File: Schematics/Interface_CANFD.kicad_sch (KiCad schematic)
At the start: 4 parts, among them U8 TCAN1044AVDRQ1

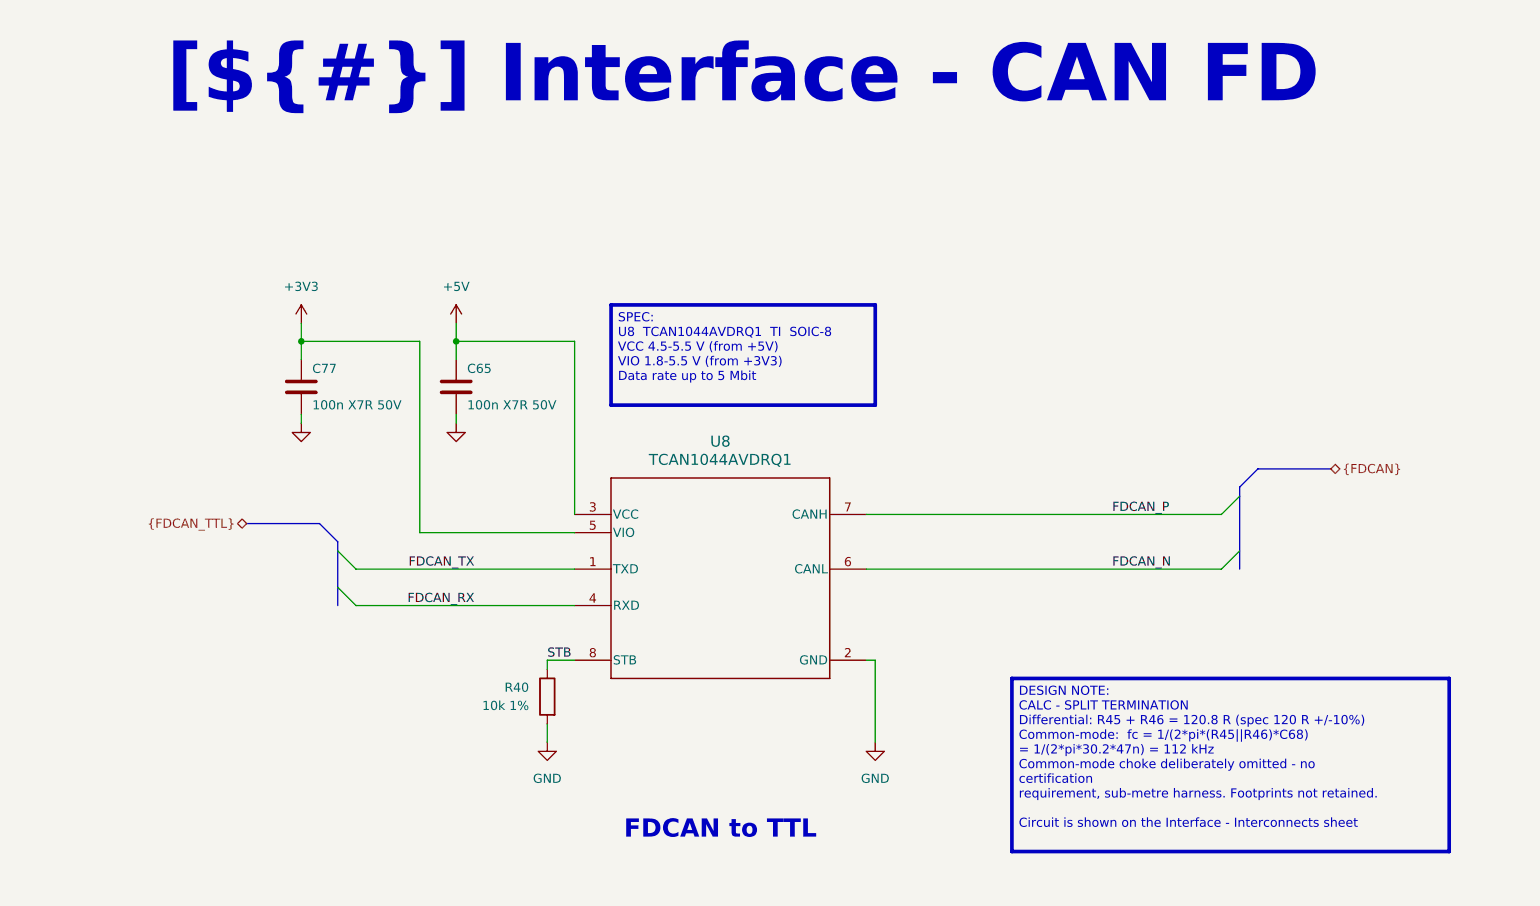
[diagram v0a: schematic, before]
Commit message: Clean up schematic design notes; export schematic and PCB artwork PDFs
- Remove firmware-only notes (boot sequence, calibration procedure,
  firmware SPI/PWM settings) and template/empty text; keep hardware facts
- Tighten wording of all DESIGN/SPEC/ASSEMBLY/REV 1 notes and resize
  boxes so no note text wraps or overflows
- Re-export schematic PDF
- Add PCB artwork PDFs (combined and one per layer: silk, paste, mask,
  L1-L6 copper), board outline on every page

Co-Authored-By: Claude Opus 5.5 <noreply@anthropic.com>
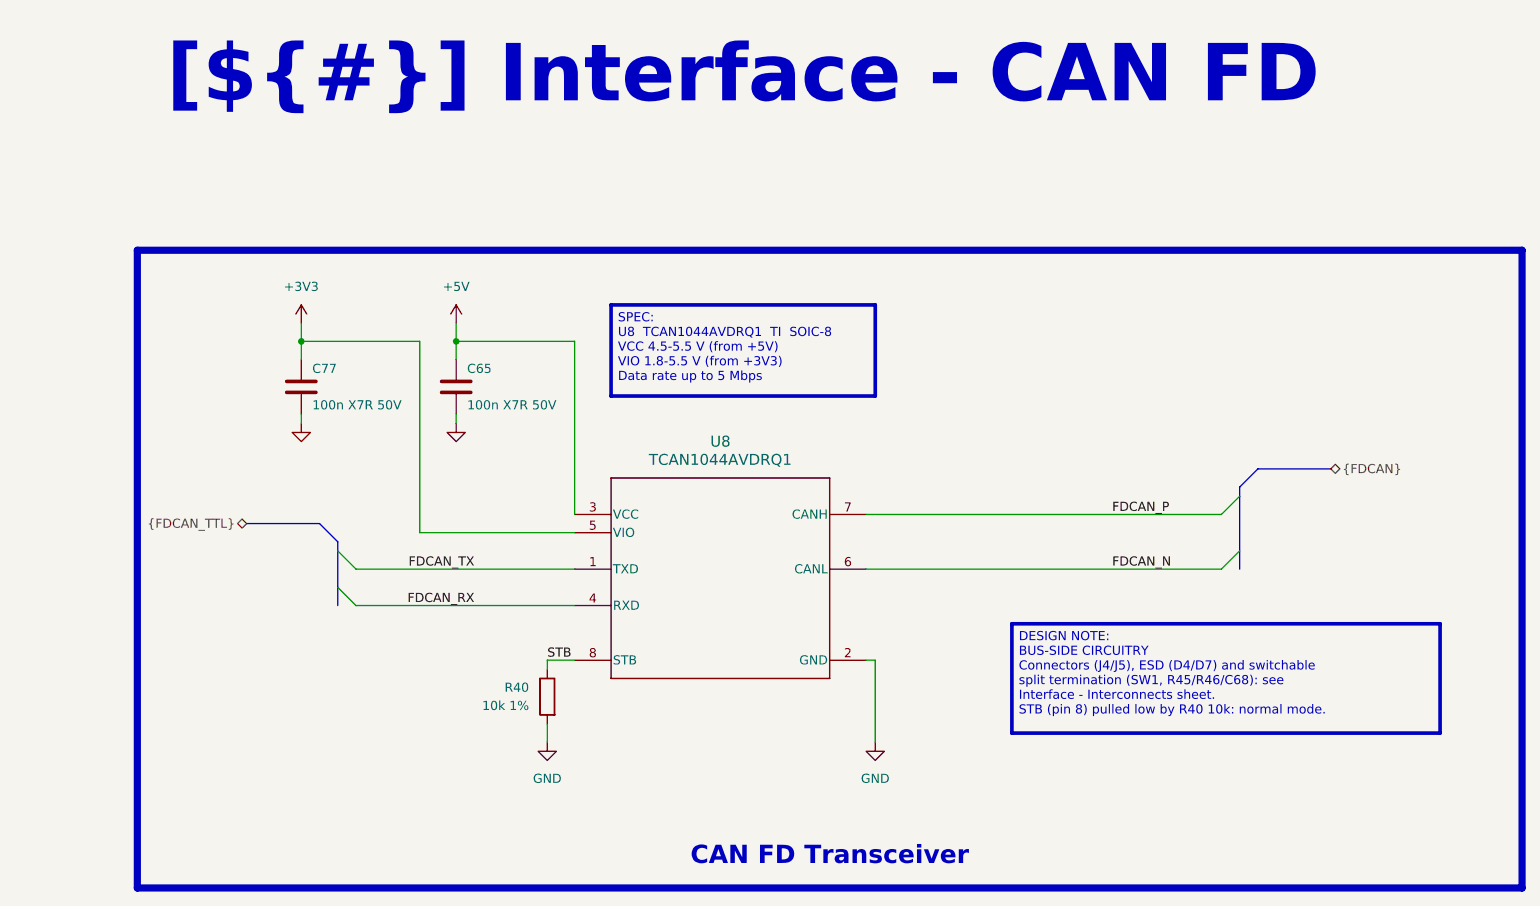
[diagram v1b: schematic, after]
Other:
- company: (none) -> ${COMPANY}
- title: (none) -> Interface - CAN FD
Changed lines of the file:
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@@
 	(generator_version "10.0")
 	(paper "A4")
+	(title_block
+		(title "Interface - CAN FD")
+		(date "${RELEASE_DATE}")
+		(rev "${REVISION}")
+		(company "${COMPANY}")
+	)
 	(text_box "[${#}] Interface - CAN FD"
 		(exclude_from_sim no)
@@
 		)
 	)
-	(text_box "FDCAN to TTL"
-		(exclude_from_sim no)
-		(at 115.57 124.46 0)
-		(size 58.42 7.7603)
-		(margins 1.9049 1.9049 1.9049 1.9049)
-		(stroke
-			(width -0.0001)
-			(type solid)
-		)
-		(fill
-			(type none)
-		)
-		(effects
-			(font
-				(face "Times New Roman")
-				(size 2.54 2.54)
-				(thickness 0.508)
-				(bold yes)
-				(color 162 22 34 1)
-			)
-			(justify bottom)
-		)
-	)
-	(text_box "DESIGN NOTE:\nCALC - SPLIT TERMINATION \nDifferential: R45 + R46 = 120.8 R (spec 120 R +/-10%) \nCommon-mode:  fc = 1/(2*pi*(R45||R46)*C68)\n                 = 1/(2*pi*30.2*47n) = 112 kHz\nCommon-mode choke deliberately omitted - no certification\nrequirement, sub-metre harness. Footprints not retained.\n\nCircuit is shown on the Interface - Interconnects sheet"
-		(exclude_from_sim no)
-		(at 185.42 107.9501 0)
-		(size 60.96 24.1299)
-		(margins 0.9525 0.9525 0.9525 0.9525)
-		(stroke
-			(width 0.508)
-			(type solid)
-			(color 0 0 255 1)
-		)
-		(fill
-			(type color)
-			(color 255 255 255 1)
-		)
-		(effects
-			(font
-				(size 1.27 1.27)
-				(color 0 0 0 1)
-			)
-			(justify left top)
-		)
-	)
-	(text_box "SPEC:\nU8  TCAN1044AVDRQ1  TI  SOIC-8\nVCC 4.5-5.5 V (from +5V) \nVIO 1.8-5.5 V (from +3V3)\nData rate up to 5 Mbit"
+	(text_box "SPEC:\nU8  TCAN1044AVDRQ1  TI  SOIC-8\nVCC 4.5-5.5 V (from +5V)\nVIO 1.8-5.5 V (from +3V3)\nData rate up to 5 Mbps"
 		(exclude_from_sim no)
 		(at 129.54 55.88 0)
-		(size 36.83 13.97)
+		(size 36.83 12.70)
 		(margins 0.9525 0.9525 0.9525 0.9525)
 		(stroke
@@
 		)
 	)
-)
+	(text_box "DESIGN NOTE:\nBUS-SIDE CIRCUITRY\nConnectors (J4/J5), ESD (D4/D7) and switchable\nsplit termination (SW1, R45/R46/C68): see\nInterface - Interconnects sheet.\nSTB (pin 8) pulled low by R40 10k: normal mode."
+		(exclude_from_sim no)
+		(at 185.42 100.33 0)
+		(size 59.69 15.24)
+		(margins 0.9525 0.9525 0.9525 0.9525)
+		(stroke
+			(width 0.508)
+			(type solid)
+			(color 0 0 255 1)
+		)
+		(fill
+			(type color)
+			(color 255 255 255 1)
+		)
+		(effects
+			(font
+				(size 1.27 1.27)
+				(color 0 0 0 1)
+			)
+			(justify left top)
+		)
+	)
+	(rectangle
+		(start 63.5 48.26)
+		(end 256.54 137.16)
+		(stroke
+			(width 1)
+			(type default)
+			(color 200 200 200 1)
+		)
+		(fill
+			(type none)
+		)
+	)
+	(text_box "CAN FD Transceiver"
+		(exclude_from_sim no)
+		(at 63.5 128.1297 0)
+		(size 193.04 7.7603)
+		(margins 1.9049 1.9049 1.9049 1.9049)
+		(stroke
+			(width -0.0001)
+			(type solid)
+		)
+		(fill
+			(type none)
+		)
+		(effects
+			(font
+				(face "Times New Roman")
+				(size 2.54 2.54)
+				(thickness 0.508)
+				(bold yes)
+				(color 162 22 34 1)
+			)
+			(justify bottom)
+		)
+	))
